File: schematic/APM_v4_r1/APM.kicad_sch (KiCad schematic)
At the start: 30 parts, among them J1 ACM_CTRL, J10 Conn_02x17_Counter_Clockwise, J13 Conn_01x06, J14 POT_FFC, J15 FPGA FFC, J18 CTRL_FFC, J2 CAN, J20 FPGA_UART, J21 FPGA FMC, J4 LCD_display, J6 Conn_02x10_Counter_Clockwise, J8 Conn_02x15_Counter_Clockwise, J9 Conn_02x08_Counter_Clockwise, U11 CD74HC4067M

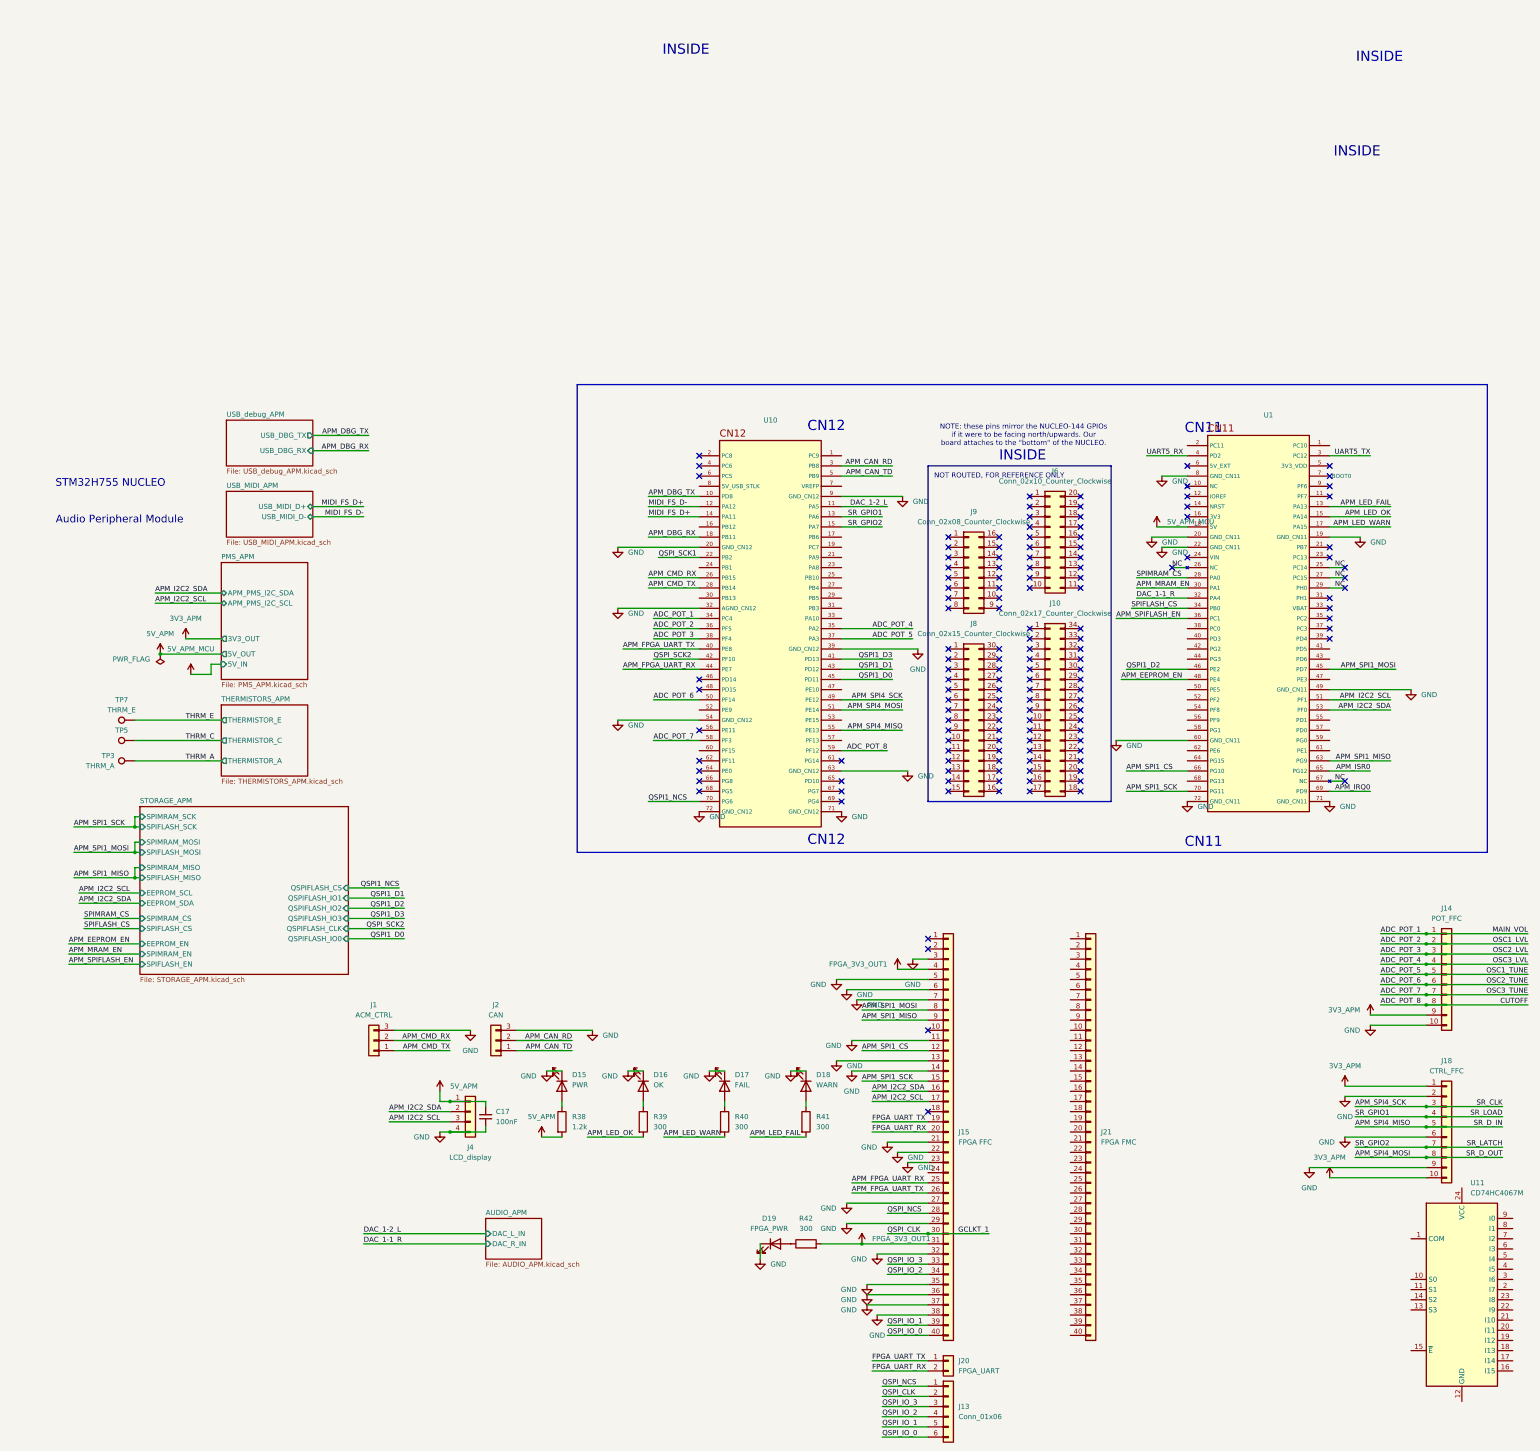
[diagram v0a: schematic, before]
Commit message: v4 routed with FPGA FMC
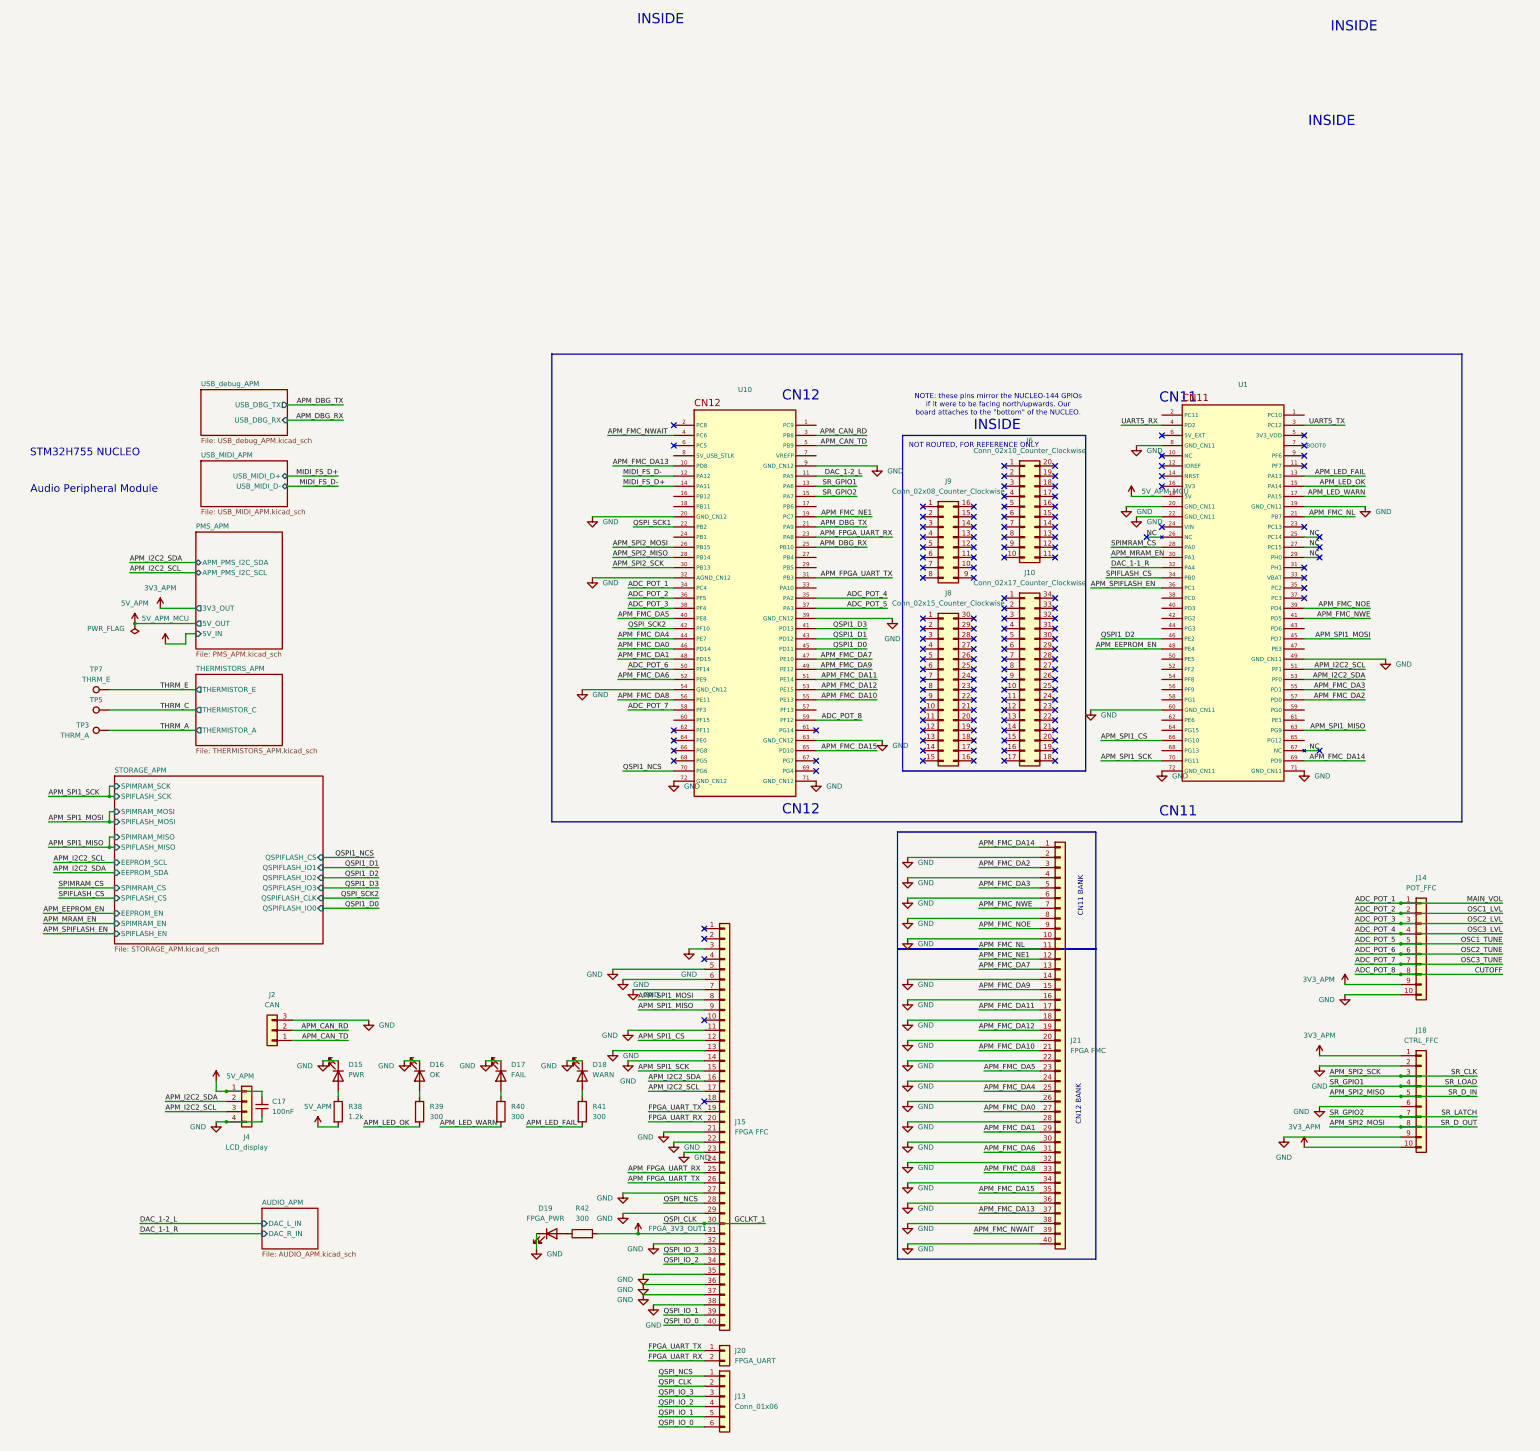
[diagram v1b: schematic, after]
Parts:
- removed J1: ACM_CTRL, Connector_PinHeader_2.54mm:PinHeader_1x03_P2.54mm_Vertical, symbol Connector_Generic:Conn_01x03
- removed U11: CD74HC4067M, Package_SO:SOIC-24W_7.5x15.4mm_P1.27mm, symbol 74xx:CD74HC4067M
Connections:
- net APM_IRQ0 is gone; now on net APM_FMC_DA14: U1.69 (PD9)
- net APM_DBG_RX: now also U10.25 (PB10); no longer U10.18 (PB11)
- net APM_DBG_TX: now also U10.21 (PA9); no longer U10.10 (PD8)
- net APM_FPGA_UART_RX: now also U10.23 (PA8); no longer U10.44 (PE7)
- net APM_FPGA_UART_TX: now also U10.31 (PB3); no longer U10.40 (PE8)
- net FPGA_3V3_OUT1: no longer J15.4 (Pin_4)
- net GND: now also J21.10 (Pin_10), J21.14 (Pin_14), J21.16 (Pin_16), J21.18 (Pin_18), J21.2 (Pin_2), J21.20 (Pin_20), J21.22 (Pin_22), J21.24 (Pin_24), J21.26 (Pin_26), J21.28 (Pin_28), J21.30 (Pin_30), J21.32 (Pin_32), J21.34 (Pin_34), J21.36 (Pin_36), J21.38 (Pin_38), J21.4 (Pin_4), J21.40 (Pin_40), J21.6 (Pin_6), J21.8 (Pin_8)
- net APM_FMC_DA14: now reaches J21.1 (Pin_1)
- net APM_FMC_NL: now reaches J21.11 (Pin_11)
- net APM_FMC_NL: now also U1.21 (PB7)
- net APM_FMC_NE1: now reaches J21.12 (Pin_12)
- net APM_FMC_NE1: now also U10.19 (PC7)
- net APM_FMC_DA7: now reaches J21.13 (Pin_13)
- net APM_FMC_DA7: now also U10.47 (PE10)
- net APM_FMC_DA9: now reaches J21.15 (Pin_15)
- net APM_FMC_DA9: now also U10.49 (PE12)
- net APM_FMC_DA11: now reaches J21.17 (Pin_17)
- net APM_FMC_DA11: now also U10.51 (PE14)
- net APM_FMC_DA12: now reaches J21.19 (Pin_19)
- net APM_FMC_DA12: now also U10.53 (PE15)
- net APM_FMC_DA10: now reaches J21.21 (Pin_21)
- net APM_FMC_DA10: now also U10.55 (PE13)
- net APM_FMC_DA5: now reaches J21.23 (Pin_23)
- net APM_FMC_DA5: now also U10.40 (PE8)
- net APM_FMC_DA4: now reaches J21.25 (Pin_25)
- net APM_FMC_DA4: now also U10.44 (PE7)
- net APM_FMC_DA0: now reaches J21.27 (Pin_27)
- net APM_FMC_DA0: now also U10.46 (PD14)
- net APM_FMC_DA1: now reaches J21.29 (Pin_29)
- net APM_FMC_DA1: now also U10.48 (PD15)
- net APM_FMC_DA2: now reaches J21.3 (Pin_3)
- net APM_FMC_DA2: now also U1.57 (PD0)
- net APM_FMC_DA6: now reaches J21.31 (Pin_31)
- net APM_FMC_DA6: now also U10.52 (PE9)
- net APM_FMC_DA8: now reaches J21.33 (Pin_33)
- net APM_FMC_DA8: now also U10.56 (PE11)
- net APM_FMC_DA15: now reaches J21.35 (Pin_35)
- net APM_FMC_DA15: now also U10.65 (PD10)
- net APM_FMC_DA13: now reaches J21.37 (Pin_37)
- net APM_FMC_DA13: now also U10.10 (PD8)
- net APM_FMC_NWAIT: now reaches J21.39 (Pin_39)
- net APM_FMC_NWAIT: now also U10.4 (PC6)
- net APM_FMC_DA3: now reaches J21.5 (Pin_5)
- net APM_FMC_DA3: now also U1.55 (PD1)
- net APM_FMC_NWE: now reaches J21.7 (Pin_7)
- net APM_FMC_NWE: now also U1.41 (PD5)
- net APM_FMC_NOE: now reaches J21.9 (Pin_9)
- net APM_FMC_NOE: now also U1.39 (PD4)
- net APM_SPI2_SCK: now reaches U10.30 (PB13)
- net APM_SPI2_SCK: now also J18.3 (Pin_3)
- net APM_CMD_RX renamed APM_SPI2_MOSI
- net APM_SPI2_MOSI: now also J18.8 (Pin_8)
- net APM_CMD_TX renamed APM_SPI2_MISO
- net APM_SPI2_MISO: now also J18.5 (Pin_5)
- net APM_ISR0: no longer names the net of U1.65 (PG12)
- removed net APM_SPI4_MISO: J18.5 (Pin_5), U10.55 (PE13)
- removed net APM_SPI4_MOSI: J18.8 (Pin_8), U10.51 (PE14)
- removed net APM_SPI4_SCK: J18.3 (Pin_3), U10.49 (PE12)
- no-connect marks 140 -> 134
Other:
- note added: "CN11 BANK"
- note added: "CN12 BANK"
- moved on the sheet: C17, D15, D16, D17, D18, D19, J10, J13, J14, J15, J18, J2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
